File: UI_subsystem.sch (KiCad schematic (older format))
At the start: 21 parts

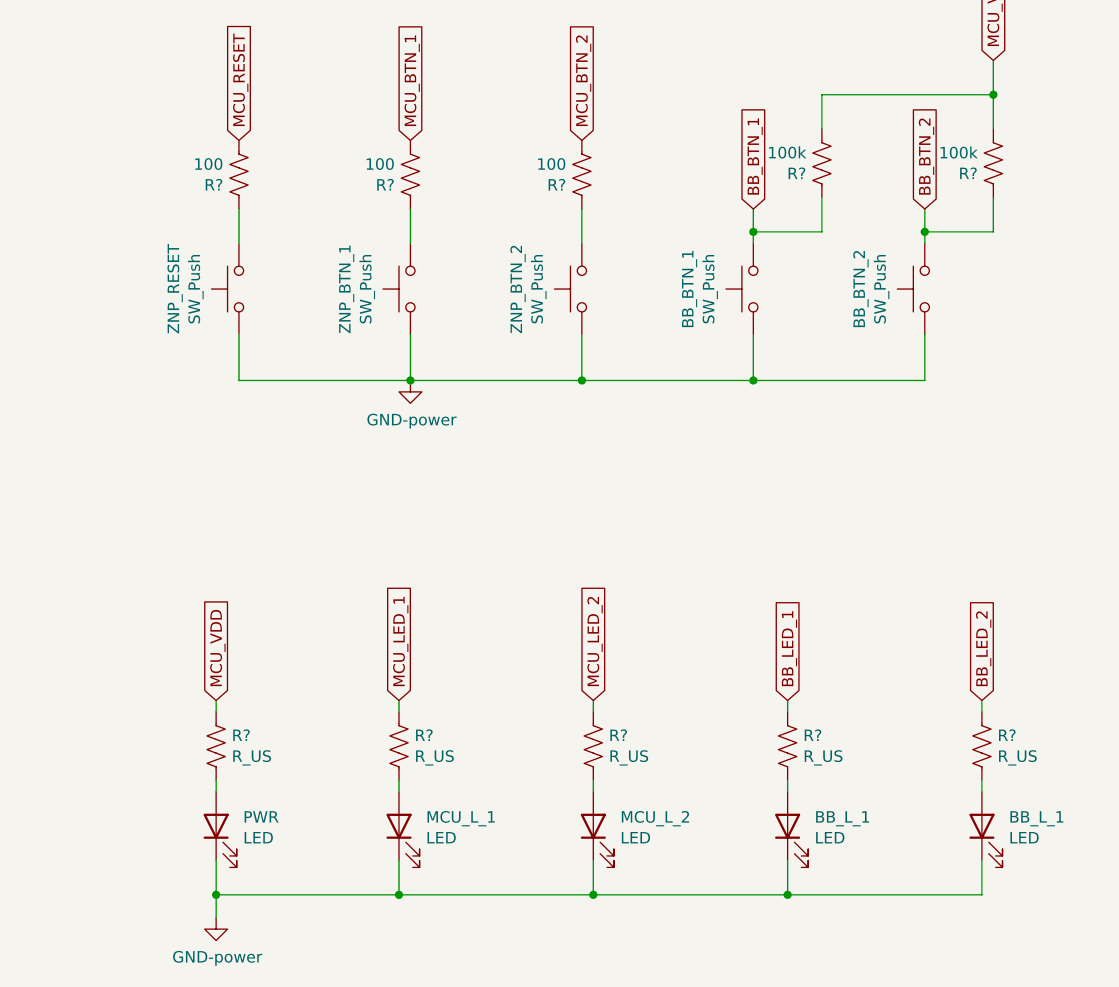
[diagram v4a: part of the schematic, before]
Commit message: part way through PCB rework using new components. 62 unconnected.
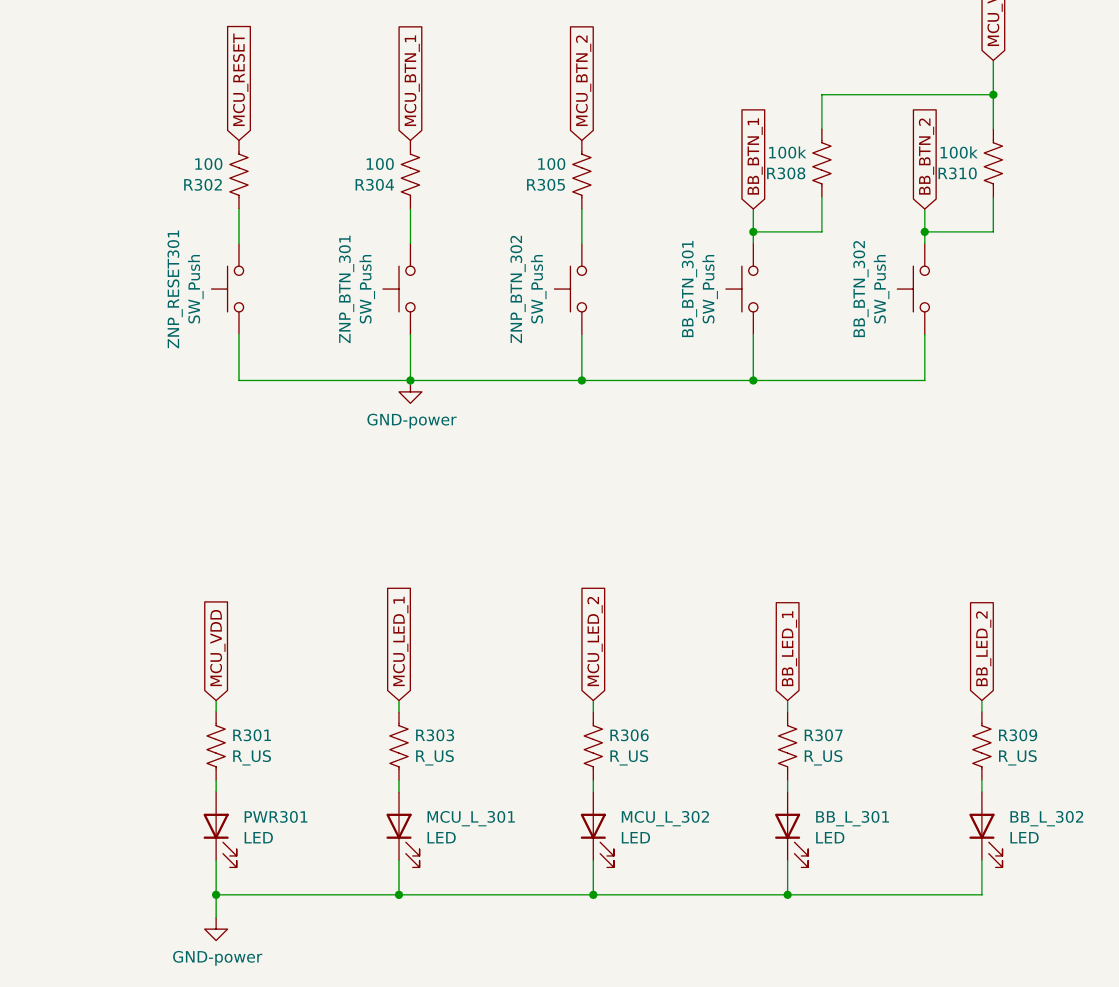
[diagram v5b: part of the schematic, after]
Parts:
- gave numbers to parts that had none: 10
- renumbered BB_BTN_1 to BB_BTN_301, BB_BTN_2 to BB_BTN_302, BB_L_1 to BB_L_301, BB_L_1 to BB_L_302, MCU_L_1 to MCU_L_301, MCU_L_2 to MCU_L_302, PWR to PWR301, ZNP_BTN_1 to ZNP_BTN_301, ZNP_BTN_2 to ZNP_BTN_302, ZNP_RESET to ZNP_RESET301
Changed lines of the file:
@@
 	3150 3550 3300 3550
 $Comp
-L Switch:SW_Push ZNP_BTN_1
+L Switch:SW_Push ZNP_BTN_301
 U 1 1 614536C0
 P 7650 2450
-F 0 "ZNP_BTN_1" H 7650 2735 50  0000 C CNN
+F 0 "ZNP_BTN_301" H 7650 2735 50  0000 C CNN
 F 1 "SW_Push" H 7650 2644 50  0000 C CNN
 F 2 "" H 7650 2650 50  0001 C CNN
@@
 $EndComp
 $Comp
-L Switch:SW_Push ZNP_BTN_2
+L Switch:SW_Push ZNP_BTN_302
 U 1 1 614542E2
 P 8400 2450
-F 0 "ZNP_BTN_2" H 8400 2735 50  0000 C CNN
+F 0 "ZNP_BTN_302" H 8400 2735 50  0000 C CNN
 F 1 "SW_Push" H 8400 2644 50  0000 C CNN
 F 2 "" H 8400 2650 50  0001 C CNN
@@
 $EndComp
 $Comp
-L Switch:SW_Push BB_BTN_1
+L Switch:SW_Push BB_BTN_301
 U 1 1 614544C6
 P 9150 2450
-F 0 "BB_BTN_1" H 9150 2735 50  0000 C CNN
+F 0 "BB_BTN_301" H 9150 2735 50  0000 C CNN
 F 1 "SW_Push" H 9150 2644 50  0000 C CNN
 F 2 "" H 9150 2650 50  0001 C CNN
@@
 $EndComp
 $Comp
-L Switch:SW_Push BB_BTN_2
+L Switch:SW_Push BB_BTN_302
 U 1 1 61454891
 P 9900 2450
-F 0 "BB_BTN_2" H 9900 2735 50  0000 C CNN
+F 0 "BB_BTN_302" H 9900 2735 50  0000 C CNN
 F 1 "SW_Push" H 9900 2644 50  0000 C CNN
 F 2 "" H 9900 2650 50  0001 C CNN
@@
 $EndComp
 $Comp
-L Device:LED PWR
+L Device:LED PWR301
 U 1 1 614557C3
 P 6800 4800
-F 0 "PWR" V 6839 4682 50  0000 R CNN
+F 0 "PWR301" V 6839 4682 50  0000 R CNN
 F 1 "LED" V 6748 4682 50  0000 R CNN
 F 2 "" H 6800 4800 50  0001 C CNN
@@
 $EndComp
 $Comp
-L Device:LED MCU_L_1
+L Device:LED MCU_L_301
 U 1 1 614568E7
 P 7600 4800
-F 0 "MCU_L_1" V 7639 4682 50  0000 R CNN
+F 0 "MCU_L_301" V 7639 4682 50  0000 R CNN
 F 1 "LED" V 7548 4682 50  0000 R CNN
 F 2 "" H 7600 4800 50  0001 C CNN
@@
 $EndComp
 $Comp
-L Device:LED MCU_L_2
+L Device:LED MCU_L_302
 U 1 1 61456F00
 P 8450 4800
-F 0 "MCU_L_2" V 8489 4682 50  0000 R CNN
+F 0 "MCU_L_302" V 8489 4682 50  0000 R CNN
 F 1 "LED" V 8398 4682 50  0000 R CNN
 F 2 "" H 8450 4800 50  0001 C CNN
@@
 $EndComp
 $Comp
-L Device:LED BB_L_1
+L Device:LED BB_L_301
 U 1 1 614573C9
 P 9300 4800
-F 0 "BB_L_1" V 9339 4682 50  0000 R CNN
+F 0 "BB_L_301" V 9339 4682 50  0000 R CNN
 F 1 "LED" V 9248 4682 50  0000 R CNN
 F 2 "" H 9300 4800 50  0001 C CNN
@@
 $EndComp
 $Comp
-L Device:LED BB_L_1
+L Device:LED BB_L_302
 U 1 1 61457651
 P 10150 4800
-F 0 "BB_L_1" V 10189 4682 50  0000 R CNN
+F 0 "BB_L_302" V 10189 4682 50  0000 R CNN
 F 1 "LED" V 10098 4682 50  0000 R CNN
 F 2 "" H 10150 4800 50  0001 C CNN
@@
 $EndComp
 $Comp
-L Device:R_US R?
+L Device:R_US R301
 U 1 1 614578E4
 P 6800 4450
-F 0 "R?" H 6868 4496 50  0000 L CNN
+F 0 "R301" H 6868 4496 50  0000 L CNN
 F 1 "R_US" H 6868 4405 50  0000 L CNN
 F 2 "" V 6840 4440 50  0001 C CNN
@@
 $EndComp
 $Comp
-L BeagleBone-Black-Cape-rescue:GND-power #PWR0301
+L BeagleBone-Black-Cape-rescue:GND-power #PWR0302
 U 1 1 61458C9B
 P 6800 5200
-F 0 "#PWR0301" H 6800 4950 50  0001 C CNN
+F 0 "#PWR0302" H 6800 4950 50  0001 C CNN
 F 1 "GND-power" H 6805 5027 50  0000 C CNN
 F 2 "" H 6800 5200 50  0001 C CNN
@@
 	6800 4950 6800 5100
 $Comp
-L Device:R_US R?
+L Device:R_US R303
 U 1 1 61463DB5
 P 7600 4450
-F 0 "R?" H 7668 4496 50  0000 L CNN
+F 0 "R303" H 7668 4496 50  0000 L CNN
 F 1 "R_US" H 7668 4405 50  0000 L CNN
 F 2 "" V 7640 4440 50  0001 C CNN
@@
 $EndComp
 $Comp
-L Device:R_US R?
+L Device:R_US R306
 U 1 1 614640E9
 P 8450 4450
-F 0 "R?" H 8518 4496 50  0000 L CNN
+F 0 "R306" H 8518 4496 50  0000 L CNN
 F 1 "R_US" H 8518 4405 50  0000 L CNN
 F 2 "" V 8490 4440 50  0001 C CNN
@@
 $EndComp
 $Comp
-L Device:R_US R?
+L Device:R_US R307
 U 1 1 614643AB
 P 9300 4450
-F 0 "R?" H 9368 4496 50  0000 L CNN
+F 0 "R307" H 9368 4496 50  0000 L CNN
 F 1 "R_US" H 9368 4405 50  0000 L CNN
 F 2 "" V 9340 4440 50  0001 C CNN
@@
 $EndComp
 $Comp
-L Device:R_US R?
+L Device:R_US R309
 U 1 1 61464797
 P 10150 4450
-F 0 "R?" H 10218 4496 50  0000 L CNN
+F 0 "R309" H 10218 4496 50  0000 L CNN
 F 1 "R_US" H 10218 4405 50  0000 L CNN
 F 2 "" V 10190 4440 50  0001 C CNN
@@
 	6800 4600 6800 4650
 $Comp
-L BeagleBone-Black-Cape-rescue:GND-power #PWR0302
+L BeagleBone-Black-Cape-rescue:GND-power #PWR0303
 U 1 1 61474E36
 P 7650 2850
-F 0 "#PWR0302" H 7650 2600 50  0001 C CNN
+F 0 "#PWR0303" H 7650 2600 50  0001 C CNN
 F 1 "GND-power" H 7655 2677 50  0000 C CNN
 F 2 "" H 7650 2850 50  0001 C CNN
@@
 $EndComp
 $Comp
-L Device:R_US R?
+L Device:R_US R304
 U 1 1 61481C85
 P 7650 1950
-F 0 "R?" H 7718 1996 50  0000 L CNN
+F 0 "R304" H 7718 1996 50  0000 L CNN
 F 1 "100" H 7718 1905 50  0000 L CNN
 F 2 "" V 7690 1940 50  0001 C CNN
@@
 Connection ~ 10200 1600
 $Comp
-L Device:R_US R?
+L Device:R_US R305
 U 1 1 61482BE5
 P 8400 1950
-F 0 "R?" H 8468 1996 50  0000 L CNN
+F 0 "R305" H 8468 1996 50  0000 L CNN
 F 1 "100" H 8468 1905 50  0000 L CNN
 F 2 "" V 8440 1940 50  0001 C CNN
@@
 $EndComp
 $Comp
-L Device:R_US R?
+L Device:R_US R308
 U 1 1 614833DA
 P 9450 1900
-F 0 "R?" H 9518 1946 50  0000 L CNN
+F 0 "R308" H 9518 1946 50  0000 L CNN
 F 1 "100k" H 9518 1855 50  0000 L CNN
 F 2 "" V 9490 1890 50  0001 C CNN
@@
 $EndComp
 $Comp
-L Device:R_US R?
+L Device:R_US R310
 U 1 1 614839E0
 P 10200 1900
-F 0 "R?" H 10268 1946 50  0000 L CNN
+F 0 "R310" H 10268 1946 50  0000 L CNN
 F 1 "100k" H 10268 1855 50  0000 L CNN
 F 2 "" V 10240 1890 50  0001 C CNN
@@
 	10200 1450 10200 1600
 $Comp
-L Switch:SW_Push ZNP_RESET
+L Switch:SW_Push ZNP_RESET301
 U 1 1 614AD723
 P 6900 2450
-F 0 "ZNP_RESET" H 6900 2735 50  0000 C CNN
+F 0 "ZNP_RESET301" H 6900 2735 50  0000 C CNN
 F 1 "SW_Push" H 6900 2644 50  0000 C CNN
 F 2 "" H 6900 2650 50  0001 C CNN
@@
 $EndComp
 $Comp
-L Device:R_US R?
+L Device:R_US R302
 U 1 1 614AD729
 P 6900 1950
-F 0 "R?" H 6968 1996 50  0000 L CNN
+F 0 "R302" H 6968 1996 50  0000 L CNN
 F 1 "100" H 6968 1905 50  0000 L CNN
 F 2 "" V 6940 1940 50  0001 C CNN
@@
 	7650 2850 6900 2850
 $Comp
-L power:GND #PWR?
+L power:GND #PWR0301
 U 1 1 614B24A7
 P 2400 2800
-F 0 "#PWR?" H 2400 2550 50  0001 C CNN
+F 0 "#PWR0301" H 2400 2550 50  0001 C CNN
 F 1 "GND" H 2405 2627 50  0000 C CNN
 F 2 "" H 2400 2800 50  0001 C CNN
